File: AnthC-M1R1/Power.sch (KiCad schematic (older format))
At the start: 30 parts, among them Q8 SI2347DS-T1-GE3, Q9 SI2347DS-T1-GE3, U1 TPS54331DR, U3 TPS78533

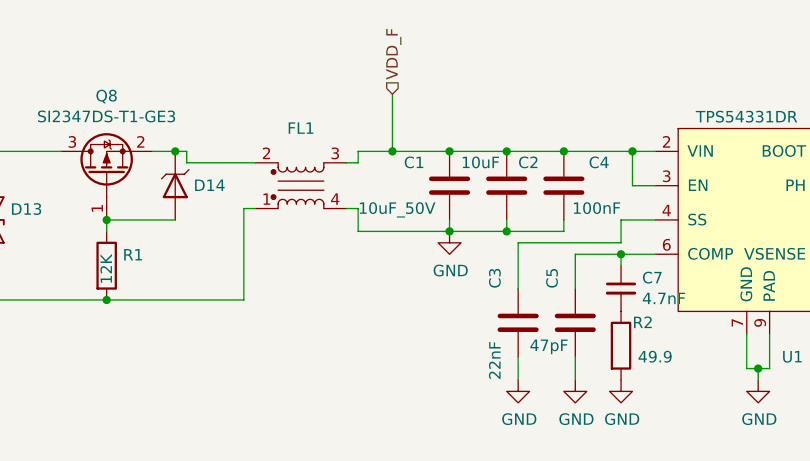
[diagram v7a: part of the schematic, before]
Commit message: Added components the libraries Replaced the battery charger for a bigger one
Optimizing layout
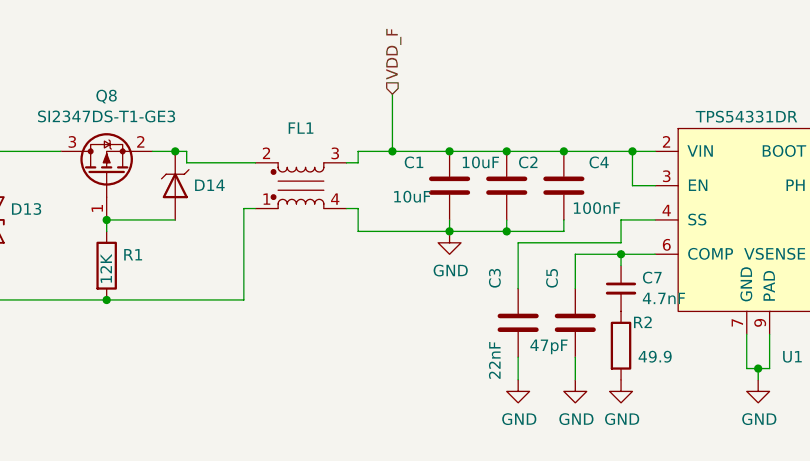
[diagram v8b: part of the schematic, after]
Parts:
- C1: value 10uF_50V -> 10uF; Description Multilayer Ceramic Capacitors MLCC - SMD/SMT 10uF+/-10% 50V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 -> Multilayer Ceramic Capacitors MLCC - SMD/SMT 10uF+/-20% 50V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; Dielectric X7R -> (none); MPN CL31B106KBHNNNE -> GRT31CR61H106ME01L; Manufacturer Samsung Electro-Mechanics -> Murata Electronics; Manufacturer Nr. CL31B106KBHNNNE -> (none); Price 0.22 -> (none); Supplier Nr. 187-CL31B106KBHNNNE -> 81-GRT31CR61H106ME1L; Tolerance 10% -> 20%
- C10, C12, C22, C9: Description Multilayer Ceramic Capacitors MLCC - SMD/SMT 47uF+/-20% 10V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 -> Multilayer Ceramic Capacitors MLCC - SMD/SMT 47uF+/-10% 10V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; Dielectric X5R -> X7R; MPN CL31A476MPHNNNE -> GRT31CR61A476KE13L; Manufacturer Samsung Electro-Mechanics -> Murata Electronics; Manufacturer Nr. CL31A476MPHNNNE -> (none); Price 0.22 -> (none); Supplier Nr. 187-CL31A476MPHNNNE -> 81-GRT31CR61A476KE3L; Tolerance 20% -> 10%
- C2: Description Multilayer Ceramic Capacitors MLCC - SMD/SMT 10uF+/-10% 50V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 -> Multilayer Ceramic Capacitors MLCC - SMD/SMT 10uF+/-20% 50V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; Dielectric X7R -> (none); MPN CL31B106KBHNNNE -> GRT31CR61H106ME01L; Manufacturer Samsung Electro-Mechanics -> Murata Electronics; Manufacturer Nr. CL31B106KBHNNNE -> (none); Price 0.22 -> (none); Supplier Nr. 187-CL31B106KBHNNNE -> 81-GRT31CR61H106ME1L; Tolerance 10% -> 20%
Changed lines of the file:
@@
 F 1 "47uF" H 7850 1900 50  0000 L CNN
 F 2 "Capacitor_SMD:C_1206_3216Metric" H 8700 2250 50  0001 C CNN
-F 3 "https://www.mouser.be/datasheet/2/585/MLCC-1837944.pdf" H 8050 2000 50  0001 C CNN
-F 4 "Samsung Electro-Mechanics" H 8350 2650 50  0001 C CNN "Manufacturer"
-F 5 "Multilayer Ceramic Capacitors MLCC - SMD/SMT 47uF+/-20% 10V X5R 1206" H 9750 2150 50  0001 C CNN "Description"
-F 6 "X5R" H 8650 2050 50  0001 C CNN "Dielectric"
-F 7 "CL31A476MPHNNNE" H 8650 2550 50  0001 C CNN "Manufacturer Nr."
-F 8 "0.22" H 9100 2050 50  0001 C CNN "Price"
-F 9 "Mouser" H 8350 2450 50  0001 C CNN "Supplier"
-F 10 "187-CL31A476MPHNNNE" H 8900 2350 50  0001 C CNN "Supplier Nr."
-F 11 "20%" H 8350 1950 50  0001 C CNN "Tolerance"
-F 12 "10V" H 8350 2050 50  0001 C CNN "Voltage"
-F 13 "CL31A476MPHNNNE" H 8050 2000 50  0001 C CNN "MPN"
+F 3 "https://www.mouser.be/datasheet/2/281/1/GRT31CR61A476KE13_01-1989683.pdf" H 8050 2000 50  0001 C CNN
+F 4 "Murata Electronics" H 8350 2650 50  0001 C CNN "Manufacturer"
+F 5 "Multilayer Ceramic Capacitors MLCC - SMD/SMT 47uF+/-10% 10V X7R 1206" H 9750 2150 50  0001 C CNN "Description"
+F 6 "X7R" H 8650 2050 50  0001 C CNN "Dielectric"
+F 7 "Mouser" H 8350 2450 50  0001 C CNN "Supplier"
+F 8 "81-GRT31CR61A476KE3L" H 8900 2350 50  0001 C CNN "Supplier Nr."
+F 9 "10%" H 8350 1950 50  0001 C CNN "Tolerance"
+F 10 "10V" H 8350 2050 50  0001 C CNN "Voltage"
+F 11 "GRT31CR61A476KE13L" H 8650 2550 50  0001 C CNN "MPN"
 	1    8050 2000
 	1    0    0    -1
@@
 F 1 "47uF" H 8900 1900 50  0000 L CNN
 F 2 "Capacitor_SMD:C_1206_3216Metric" H 9800 2250 50  0001 C CNN
-F 3 "https://www.mouser.be/datasheet/2/585/MLCC-1837944.pdf" H 9150 2000 50  0001 C CNN
-F 4 "Samsung Electro-Mechanics" H 9450 2650 50  0001 C CNN "Manufacturer"
-F 5 "Multilayer Ceramic Capacitors MLCC - SMD/SMT 47uF+/-20% 10V X5R 1206" H 10850 2150 50  0001 C CNN "Description"
-F 6 "X5R" H 9750 2050 50  0001 C CNN "Dielectric"
-F 7 "CL31A476MPHNNNE" H 9750 2550 50  0001 C CNN "Manufacturer Nr."
-F 8 "0.22" H 10200 2050 50  0001 C CNN "Price"
-F 9 "Mouser" H 9450 2450 50  0001 C CNN "Supplier"
-F 10 "187-CL31A476MPHNNNE" H 10000 2350 50  0001 C CNN "Supplier Nr."
-F 11 "20%" H 9450 1950 50  0001 C CNN "Tolerance"
-F 12 "10V" H 9450 2050 50  0001 C CNN "Voltage"
-F 13 "CL31A476MPHNNNE" H 9150 2000 50  0001 C CNN "MPN"
+F 3 "https://www.mouser.be/datasheet/2/281/1/GRT31CR61A476KE13_01-1989683.pdf" H 9150 2000 50  0001 C CNN
+F 4 "Murata Electronics" H 9450 2650 50  0001 C CNN "Manufacturer"
+F 5 "Multilayer Ceramic Capacitors MLCC - SMD/SMT 47uF+/-10% 10V X7R 1206" H 10850 2150 50  0001 C CNN "Description"
+F 6 "X7R" H 9750 2050 50  0001 C CNN "Dielectric"
+F 7 "Mouser" H 9450 2450 50  0001 C CNN "Supplier"
+F 8 "81-GRT31CR61A476KE3L" H 10000 2350 50  0001 C CNN "Supplier Nr."
+F 9 "10%" H 9450 1950 50  0001 C CNN "Tolerance"
+F 10 "10V" H 9450 2050 50  0001 C CNN "Voltage"
+F 11 "GRT31CR61A476KE13L" H 9750 2550 50  0001 C CNN "MPN"
 	1    9150 2000
 	1    0    0    -1
@@
 F 1 "10uF" H 2900 1700 50  0000 L CNN
 F 2 "Capacitor_SMD:C_1206_3216Metric" H 4400 1800 50  0001 C CNN
-F 3 "https://www.mouser.be/datasheet/2/585/MLCC-1837944.pdf" H 3100 1600 50  0001 C CNN
-F 4 "Samsung Electro-Mechanics" H 4200 2550 50  0001 C CNN "Manufacturer"
-F 5 "Multilayer Ceramic Capacitors MLCC - SMD/SMT 10uF+/-10% 50V X7R 3216" H 4800 1750 50  0001 C CNN "Description"
-F 6 "X7R" H 3700 1650 50  0001 C CNN "Dielectric"
-F 7 "CL31B106KBHNNNE" H 4150 2100 50  0001 C CNN "Manufacturer Nr."
-F 8 "0.22" H 4150 1650 50  0001 C CNN "Price"
-F 9 "Mouser" H 3900 2000 50  0001 C CNN "Supplier"
-F 10 "187-CL31B106KBHNNNE" H 3950 1950 50  0001 C CNN "Supplier Nr."
-F 11 "10%" H 3400 1550 50  0001 C CNN "Tolerance"
-F 12 "50V" H 3400 1650 50  0001 C CNN "Voltage"
-F 13 "CL31B106KBHNNNE" H 3100 1600 50  0001 C CNN "MPN"
+F 3 "https://www.mouser.be/datasheet/2/281/GRT31CR61H106ME01-01-1065064.pdf" H 3100 1600 50  0001 C CNN
+F 4 "Murata Electronics" H 4200 2550 50  0001 C CNN "Manufacturer"
+F 5 "Multilayer Ceramic Capacitors MLCC - SMD/SMT 10uF+/-20% 50V X5R 1206" H 4800 1750 50  0001 C CNN "Description"
+F 6 "Mouser" H 3900 2000 50  0001 C CNN "Supplier"
+F 7 "81-GRT31CR61H106ME1L" H 3950 1950 50  0001 C CNN "Supplier Nr."
+F 8 "20%" H 3400 1550 50  0001 C CNN "Tolerance"
+F 9 "50V" H 3400 1650 50  0001 C CNN "Voltage"
+F 10 "GRT31CR61H106ME01L" H 3100 1600 50  0001 C CNN "MPN"
 	1    3100 1600
 	1    0    0    -1
@@
 F 1 "47uF" H 5250 1750 50  0000 L CNN
 F 2 "Capacitor_SMD:C_1206_3216Metric" H 6100 2100 50  0001 C CNN
-F 3 "https://www.mouser.be/datasheet/2/585/MLCC-1837944.pdf" H 5450 1850 50  0001 C CNN
-F 4 "Samsung Electro-Mechanics" H 5750 2500 50  0001 C CNN "Manufacturer"
-F 5 "Multilayer Ceramic Capacitors MLCC - SMD/SMT 47uF+/-20% 10V X5R 1206" H 7150 2000 50  0001 C CNN "Description"
-F 6 "X5R" H 6050 1900 50  0001 C CNN "Dielectric"
-F 7 "CL31A476MPHNNNE" H 6050 2400 50  0001 C CNN "Manufacturer Nr."
-F 8 "0.22" H 6500 1900 50  0001 C CNN "Price"
-F 9 "Mouser" H 5750 2300 50  0001 C CNN "Supplier"
-F 10 "187-CL31A476MPHNNNE" H 6300 2200 50  0001 C CNN "Supplier Nr."
-F 11 "20%" H 5750 1800 50  0001 C CNN "Tolerance"
-F 12 "10V" H 5750 1900 50  0001 C CNN "Voltage"
-F 13 "CL31A476MPHNNNE" H 5450 1850 50  0001 C CNN "MPN"
+F 3 "https://www.mouser.be/datasheet/2/281/1/GRT31CR61A476KE13_01-1989683.pdf" H 5450 1850 50  0001 C CNN
+F 4 "Murata Electronics" H 5750 2500 50  0001 C CNN "Manufacturer"
+F 5 "Multilayer Ceramic Capacitors MLCC - SMD/SMT 47uF+/-10% 10V X7R 1206" H 7150 2000 50  0001 C CNN "Description"
+F 6 "X7R" H 6050 1900 50  0001 C CNN "Dielectric"
+F 7 "Mouser" H 5750 2300 50  0001 C CNN "Supplier"
+F 8 "81-GRT31CR61A476KE3L" H 6300 2200 50  0001 C CNN "Supplier Nr."
+F 9 "10%" H 5750 1800 50  0001 C CNN "Tolerance"
+F 10 "10V" H 5750 1900 50  0001 C CNN "Voltage"
+F 11 "GRT31CR61A476KE13L" H 5450 1850 50  0001 C CNN "MPN"
 	1    5450 1850
 	1    0    0    -1
@@
 AR Path="/6243F6D9/6269B4F8" Ref="C1"  Part="1"
 F 0 "C1" H 2650 1700 50  0000 L CNN
-F 1 "10uF_50V" H 2450 1500 50  0000 L CNN
+F 1 "10uF" H 2600 1550 50  0000 L CNN
 F 2 "Capacitor_SMD:C_1206_3216Metric" H 4150 1800 50  0001 C CNN
-F 3 "https://www.mouser.be/datasheet/2/585/MLCC-1837944.pdf" H 2850 1600 50  0001 C CNN
-F 4 "Samsung Electro-Mechanics" H 3950 2550 50  0001 C CNN "Manufacturer"
-F 5 "Multilayer Ceramic Capacitors MLCC - SMD/SMT 10uF+/-10% 50V X7R 3216" H 4550 1750 50  0001 C CNN "Description"
-F 6 "X7R" H 3450 1650 50  0001 C CNN "Dielectric"
-F 7 "CL31B106KBHNNNE" H 3900 2100 50  0001 C CNN "Manufacturer Nr."
-F 8 "0.22" H 3900 1650 50  0001 C CNN "Price"
-F 9 "Mouser" H 3650 2000 50  0001 C CNN "Supplier"
-F 10 "187-CL31B106KBHNNNE" H 3700 1950 50  0001 C CNN "Supplier Nr."
-F 11 "10%" H 3150 1550 50  0001 C CNN "Tolerance"
-F 12 "50V" H 3150 1650 50  0001 C CNN "Voltage"
-F 13 "CL31B106KBHNNNE" H 2850 1600 50  0001 C CNN "MPN"
+F 3 "https://www.mouser.be/datasheet/2/281/GRT31CR61H106ME01-01-1065064.pdf" H 2850 1600 50  0001 C CNN
+F 4 "Murata Electronics" H 3950 2550 50  0001 C CNN "Manufacturer"
+F 5 "Multilayer Ceramic Capacitors MLCC - SMD/SMT 10uF+/-20% 50V X5R 1206" H 4550 1750 50  0001 C CNN "Description"
+F 6 "Mouser" H 3650 2000 50  0001 C CNN "Supplier"
+F 7 "81-GRT31CR61H106ME1L" H 3700 1950 50  0001 C CNN "Supplier Nr."
+F 8 "20%" H 3150 1550 50  0001 C CNN "Tolerance"
+F 9 "50V" H 3150 1650 50  0001 C CNN "Voltage"
+F 10 "GRT31CR61H106ME01L" H 2850 1600 50  0001 C CNN "MPN"
 	1    2850 1600
 	1    0    0    -1
@@
 F 1 "47uF" H 5000 1750 50  0000 L CNN
 F 2 "Capacitor_SMD:C_1206_3216Metric" H 5850 2100 50  0001 C CNN
-F 3 "https://www.mouser.be/datasheet/2/585/MLCC-1837944.pdf" H 5200 1850 50  0001 C CNN
-F 4 "Samsung Electro-Mechanics" H 5500 2500 50  0001 C CNN "Manufacturer"
-F 5 "Multilayer Ceramic Capacitors MLCC - SMD/SMT 47uF+/-20% 10V X5R 1206" H 6900 2000 50  0001 C CNN "Description"
-F 6 "X5R" H 5800 1900 50  0001 C CNN "Dielectric"
-F 7 "CL31A476MPHNNNE" H 5800 2400 50  0001 C CNN "Manufacturer Nr."
-F 8 "0.22" H 6250 1900 50  0001 C CNN "Price"
-F 9 "Mouser" H 5500 2300 50  0001 C CNN "Supplier"
-F 10 "187-CL31A476MPHNNNE" H 6050 2200 50  0001 C CNN "Supplier Nr."
-F 11 "20%" H 5500 1800 50  0001 C CNN "Tolerance"
-F 12 "10V" H 5500 1900 50  0001 C CNN "Voltage"
-F 13 "CL31A476MPHNNNE" H 5200 1850 50  0001 C CNN "MPN"
+F 3 "https://www.mouser.be/datasheet/2/281/1/GRT31CR61A476KE13_01-1989683.pdf" H 5200 1850 50  0001 C CNN
+F 4 "Murata Electronics" H 5500 2500 50  0001 C CNN "Manufacturer"
+F 5 "Multilayer Ceramic Capacitors MLCC - SMD/SMT 47uF+/-10% 10V X7R 1206" H 6900 2000 50  0001 C CNN "Description"
+F 6 "X7R" H 5800 1900 50  0001 C CNN "Dielectric"
+F 7 "Mouser" H 5500 2300 50  0001 C CNN "Supplier"
+F 8 "81-GRT31CR61A476KE3L" H 6050 2200 50  0001 C CNN "Supplier Nr."
+F 9 "10%" H 5500 1800 50  0001 C CNN "Tolerance"
+F 10 "10V" H 5500 1900 50  0001 C CNN "Voltage"
+F 11 "GRT31CR61A476KE13L" H 5200 1850 50  0001 C CNN "MPN"
 	1    5200 1850
 	1    0    0    -1
